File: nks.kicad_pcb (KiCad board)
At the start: 2 copper layers, 80 x 90 mm, 18 parts, among them J1 microSD, J2 DevKit-J1, J3 DevKit-J3, SW1 SW_Push, U2 RTC_DS3231+AT24C32, U3 SHT30

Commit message: feat(sw1): interruptor SPDT (SS12D00) rutado y verificado DRC 0; elimina R2 pull-up; anade libreria de footprints propia nks.pretty
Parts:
- removed R2: 10k, Resistor_SMD:R_0805_2012Metric
- SW1: value SW_Push -> SW_SPDT; footprint Button_Switch_THT:SW_PUSH_6mm -> nks:SS12D00
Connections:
- SW1 pad 1: /BTN -> /+3V3
- SW1 pad 2: /GND -> /BTN
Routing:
- net /+3V3: track 252.6 -> 245.5 mm
- net /BTN: track 234.4 -> 235.3 mm

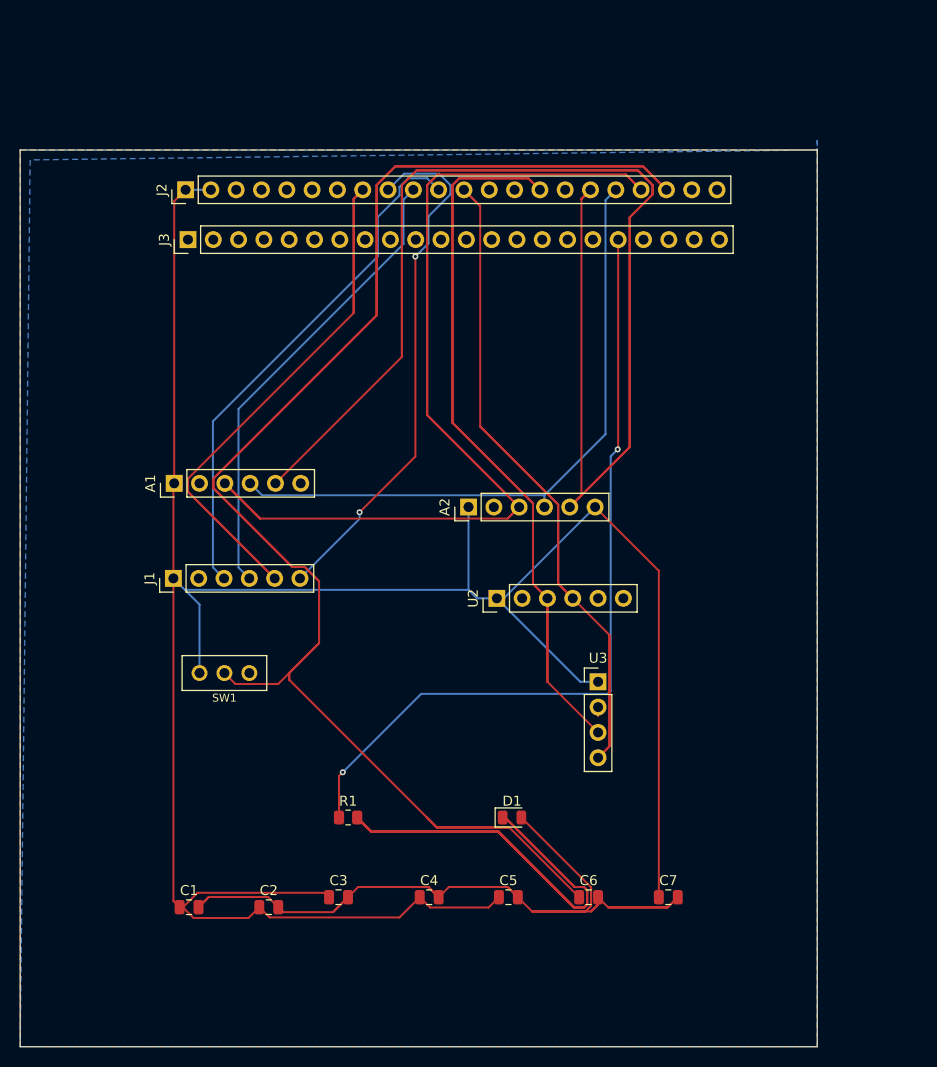
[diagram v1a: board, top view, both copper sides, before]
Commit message: layout: reconstruccion PCB desde esquematico nuevo - 20 componentes colocados, DevKit orientado USB trasero, panel LED+switch frontal
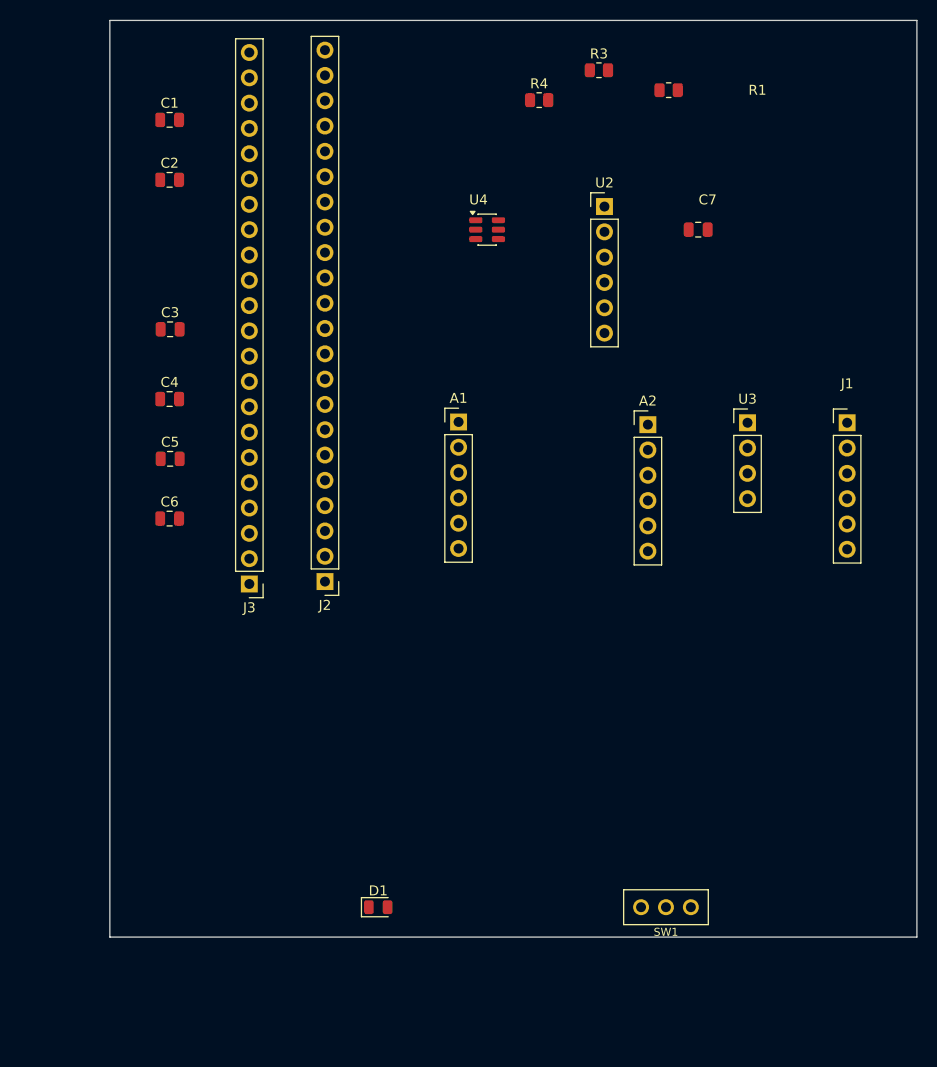
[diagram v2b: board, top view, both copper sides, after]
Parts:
- added R3: 100k, Resistor_SMD:R_0805_2012Metric, F.Cu at (149.1, 44.0)
- added R4: 100k, Resistor_SMD:R_0805_2012Metric, F.Cu at (143.1, 47.0)
- added U4: TPS22918, Package_TO_SOT_SMD:SOT-23-6, F.Cu at (137.9, 60.0)
- moved R1 79.8 mm to (156.1, 46.0)
- moved C1 79.0 mm to (106.0, 49.0)
- moved C2 73.7 mm to (106.0, 55.0)
- moved J1 69.4 mm to (174.0, 79.4), turned to 0 degrees
- moved C7 67.1 mm to (159.1, 60.0)
- moved C3 59.5 mm to (106.0, 70.0)
- moved C6 56.7 mm to (106.0, 89.0)
- moved C4 56.4 mm to (106.0, 77.0)
- moved C5 55.6 mm to (106.0, 83.0)
- moved SW1 50.2 mm to (155.8, 128.0)
- moved J2 41.7 mm to (121.6, 95.3), turned to 180 degrees
- moved U2 40.8 mm to (149.6, 57.7), turned to 0 degrees
- moved J3 35.1 mm to (114.0, 95.6), turned to 180 degrees
- moved U3 30.0 mm to (164.0, 79.4)
- moved A1 29.2 mm to (135.0, 79.3), turned to 0 degrees
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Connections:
- A1 pad 1: /+3V3 -> /+3V3_SW
- A2 pad 1: /+3V3 -> /+3V3_SW
- A2 pad 6: /+3V3 -> /+3V3_SW
- C1 pad 1: /+3V3 -> /+3V3_SW
- C2 pad 1: /+3V3 -> /+3V3_SW
- C3 pad 1: /+3V3 -> /+3V3_SW
- C4 pad 1: /+3V3 -> /+3V3_SW
- C5 pad 1: /+3V3 -> /+3V3_SW
- C7 pad 1: /+3V3 -> /+3V3_IN
- J1 pad 1: /+3V3 -> /+3V3_SW
- J2 pad 1: /+3V3 -> /+3V3_IN
- J2 pad 2: /+3V3 -> /+3V3_IN
- J2 pad 21: (no net) -> /VBUS
- J2 pad 4: (no net) -> /ENABLE
- J2 pad 5: (no net) -> /VBUS_ADC
- SW1 pad 1: /+3V3 -> /+3V3_SW
- U2 pad 1: /+3V3 -> /+3V3_IN
- U3 pad 1: /+3V3 -> /+3V3_SW
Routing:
- net /+3V3: track 245.5 -> 0.00 mm
- net /BTN: track 235.3 -> 0.00 mm
- net /LED_A: track 235.2 -> 0.00 mm
- net /I2S_WS: track 212.4 -> 0.00 mm
- net /I2S_SD: track 136.7 -> 0.00 mm
- net /I2C_SCL: track 125.8 -> 0.00 mm
- net /GND: track 116.0 -> 0.00 mm
- net /I2C_SDA: track 99.7 -> 0.00 mm
- net /LED_STAT: track 80.6 -> 0.00 mm, vias 2 -> 0
- net /SD_MOSI: track 74.9 -> 0.00 mm
- net /I2S_SCK: track 65.6 -> 0.00 mm
- net /SD_MISO: track 53.1 -> 0.00 mm, vias 2 -> 0
- net /SD_CS: track 52.3 -> 0.00 mm
- net /SD_SCLK: track 46.7 -> 0.00 mm
- removed copper zone on B.Cu, net /GND
- removed copper zone on F.Cu, net /GND
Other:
- board size 80 x 90 mm -> 81 x 92 mm

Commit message: layout: planos GND ambas caras rellenados (58->38 sin conectar); recupera ficheros tras restauracion KiCad
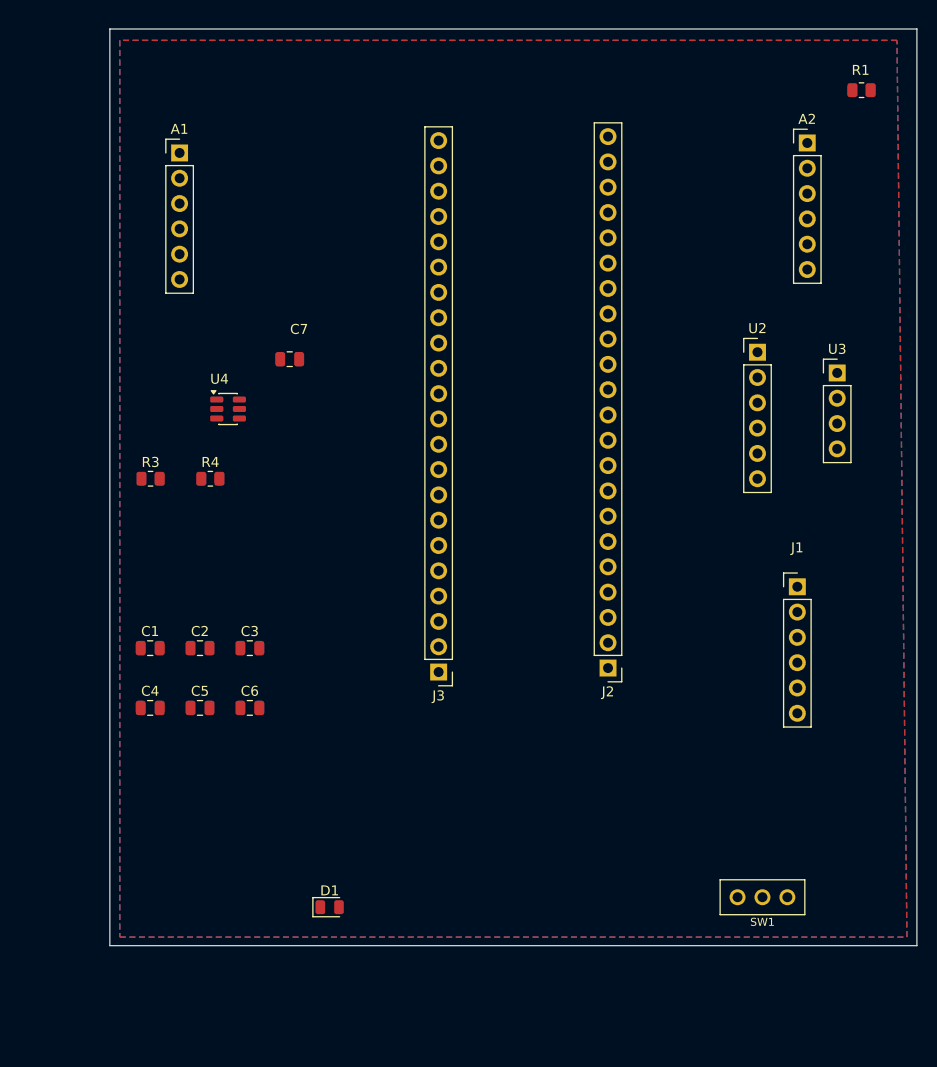
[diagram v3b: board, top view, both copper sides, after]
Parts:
- moved R3 60.9 mm to (104.1, 85.0)
- moved C1 53.1 mm to (104.0, 102.0)
- moved R4 50.3 mm to (110.1, 85.0)
- moved C2 47.1 mm to (109.0, 102.0)
- moved C7 43.0 mm to (118.0, 73.0)
- moved A1 38.9 mm to (107.0, 52.3)
- moved C3 33.0 mm to (114.0, 102.0)
- moved A2 32.5 mm to (170.0, 51.3)
- moved U4 31.6 mm to (111.9, 78.0)
- moved C4 31.1 mm to (104.0, 108.0)
- moved J2 29.7 mm to (150.0, 104.0)
- moved C5 25.2 mm to (109.0, 108.0)
- moved U2 21.2 mm to (165.0, 72.3)
- moved J3 21.0 mm to (133.0, 104.4)
- moved C6 20.6 mm to (114.0, 108.0)
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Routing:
- added copper zone on B.Cu, net /GND
- added copper zone on F.Cu, net /GND
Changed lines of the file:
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@@
 	(footprint "nks:SS12D00"
 		(layer "F.Cu")
-		(at 155.815 128)
+		(at 165.5 127)
 		(property "Reference" "SW1"
 			(at 0 2.5 0)
@@
 	(footprint "Capacitor_SMD:C_0805_2012Metric"
 		(layer "F.Cu")
-		(at 106 55)
+		(at 109.05 102)
 		(descr "Capacitor SMD 0805 (2012 Metric), square (rectangular) end terminal, IPC-7351 nominal, (Body size source: IPC-SM-782 page 76, https://www.pcb-3d.com/wordpress/wp-content/uploads/ipc-sm-782a_amendment_1_and_2.pdf, https://docs.google.com/spreadsheets/d/1BsfQQcO9C6DZCsRaXUlFlo91Tg2WpOkGARC1WS5S8t0/edit?usp=sharing)")
 		(tags "capacitor")
@@
 	(footprint "Connector_PinHeader_2.54mm:PinHeader_1x22_P2.54mm_Vertical"
 		(layer "F.Cu")
-		(at 114 95.56 180)
+		(at 133 104.4 180)
 		(descr "Through hole straight pin header, 1x22, 2.54mm pitch, single row")
 		(tags "Through hole pin header THT 1x22 2.54mm single row")
@@
 		)
 		(property "Value" "DevKit-J3"
-			(at 0 55.72 0)
+			(at 0 56.4 0)
 			(layer "F.Fab")
 			(effects
@@
 	(footprint "Connector_PinHeader_2.54mm:PinHeader_1x06_P2.54mm_Vertical"
 		(layer "F.Cu")
-		(at 135 79.3)
+		(at 107 52.3)
 		(descr "Through hole straight pin header, 1x06, 2.54mm pitch, single row")
 		(tags "Through hole pin header THT 1x06 2.54mm single row")
@@
 	(footprint "Connector_PinHeader_2.54mm:PinHeader_1x06_P2.54mm_Vertical"
 		(layer "F.Cu")
-		(at 174 79.38)
+		(at 169 95.84)
 		(descr "Through hole straight pin header, 1x06, 2.54mm pitch, single row")
 		(tags "Through hole pin header THT 1x06 2.54mm single row")
@@
 	(footprint "Connector_PinHeader_2.54mm:PinHeader_1x22_P2.54mm_Vertical"
 		(layer "F.Cu")
-		(at 121.59 95.32 180)
+		(at 150 104 180)
 		(descr "Through hole straight pin header, 1x22, 2.54mm pitch, single row")
 		(tags "Through hole pin header THT 1x22 2.54mm single row")
@@
 		)
 		(property "Value" "DevKit-J1"
-			(at 0 55.72 0)
+			(at 0 56 0)
 			(layer "F.Fab")
 			(effects
@@
 	(footprint "Connector_PinHeader_2.54mm:PinHeader_1x04_P2.54mm_Vertical"
 		(layer "F.Cu")
-		(at 164 79.38)
+		(at 173 74.38)
 		(descr "Through hole straight pin header, 1x04, 2.54mm pitch, single row")
 		(tags "Through hole pin header THT 1x04 2.54mm single row")
@@
 	(footprint "Resistor_SMD:R_0805_2012Metric"
 		(layer "F.Cu")
-		(at 143.0875 47)
+		(at 110.0875 85)
 		(descr "Resistor SMD 0805 (2012 Metric), square (rectangular) end terminal, IPC-7351 nominal, (Body size source: IPC-SM-782 page 72, https://www.pcb-3d.com/wordpress/wp-content/uploads/ipc-sm-782a_amendment_1_and_2.pdf)")
 		(tags "resistor")
@@
 	(footprint "Capacitor_SMD:C_0805_2012Metric"
 		(layer "F.Cu")
-		(at 106.05 70)
+		(at 114.05 102)
 		(descr "Capacitor SMD 0805 (2012 Metric), square (rectangular) end terminal, IPC-7351 nominal, (Body size source: IPC-SM-782 page 76, https://www.pcb-3d.com/wordpress/wp-content/uploads/ipc-sm-782a_amendment_1_and_2.pdf, https://docs.google.com/spreadsheets/d/1BsfQQcO9C6DZCsRaXUlFlo91Tg2WpOkGARC1WS5S8t0/edit?usp=sharing)")
 		(tags "capacitor")
@@
 	(footprint "Connector_PinHeader_2.54mm:PinHeader_1x06_P2.54mm_Vertical"
 		(layer "F.Cu")
-		(at 149.643748 57.68)
+		(at 165 72.3)
 		(descr "Through hole straight pin header, 1x06, 2.54mm pitch, single row")
 		(tags "Through hole pin header THT 1x06 2.54mm single row")
@@
 	(footprint "Package_TO_SOT_SMD:SOT-23-6"
 		(layer "F.Cu")
-		(at 137.8625 60)
+		(at 111.8625 78)
 		(descr "SOT, 6 Pin (JEDEC MO-178 Var AB https://www.jedec.org/document_search?search_api_views_fulltext=MO-178)")
 		(tags "SOT TO_SOT_SMD")
@@
 	(footprint "Resistor_SMD:R_0805_2012Metric"
 		(layer "F.Cu")
-		(at 149.0875 44)
+		(at 104.0875 85)
 		(descr "Resistor SMD 0805 (2012 Metric), square (rectangular) end terminal, IPC-7351 nominal, (Body size source: IPC-SM-782 page 72, https://www.pcb-3d.com/wordpress/wp-content/uploads/ipc-sm-782a_amendment_1_and_2.pdf)")
 		(tags "resistor")
@@
 	(footprint "Capacitor_SMD:C_0805_2012Metric"
 		(layer "F.Cu")
-		(at 106 89)
+		(at 114.05 108)
 		(descr "Capacitor SMD 0805 (2012 Metric), square (rectangular) end terminal, IPC-7351 nominal, (Body size source: IPC-SM-782 page 76, https://www.pcb-3d.com/wordpress/wp-content/uploads/ipc-sm-782a_amendment_1_and_2.pdf, https://docs.google.com/spreadsheets/d/1BsfQQcO9C6DZCsRaXUlFlo91Tg2WpOkGARC1WS5S8t0/edit?usp=sharing)")
 		(tags "capacitor")
@@
 	(footprint "LED_SMD:LED_0805_2012Metric"
 		(layer "F.Cu")
-		(at 126.9375 128)
+		(at 122.0625 128)
 		(descr "LED SMD 0805 (2012 Metric), square (rectangular) end terminal, IPC-7351 nominal, (Body size source: https://docs.google.com/spreadsheets/d/1BsfQQcO9C6DZCsRaXUlFlo91Tg2WpOkGARC1WS5S8t0/edit?usp=sharing)")
 		(tags "LED")
@@
 	(footprint "Resistor_SMD:R_0805_2012Metric"
 		(layer "F.Cu")
-		(at 156.0875 46)
+		(at 175.443752 46)
 		(descr "Resistor SMD 0805 (2012 Metric), square (rectangular) end terminal, IPC-7351 nominal, (Body size source: IPC-SM-782 page 72, https://www.pcb-3d.com/wordpress/wp-content/uploads/ipc-sm-782a_amendment_1_and_2.pdf)")
 		(tags "resistor")
 		(property "Reference" "R1"
-			(at 8.9125 0 0)
+			(at -0.0875 -2 0)
 			(layer "F.SilkS")
 			(effects
@@
 	(footprint "Connector_PinHeader_2.54mm:PinHeader_1x06_P2.54mm_Vertical"
 		(layer "F.Cu")
-		(at 154 79.57)
+		(at 170 51.3)
 		(descr "Through hole straight pin header, 1x06, 2.54mm pitch, single row")
 		(tags "Through hole pin header THT 1x06 2.54mm single row")
@@
 	(footprint "Capacitor_SMD:C_0805_2012Metric"
 		(layer "F.Cu")
-		(at 106 77)
+		(at 104.05 108)
 		(descr "Capacitor SMD 0805 (2012 Metric), square (rectangular) end terminal, IPC-7351 nominal, (Body size source: IPC-SM-782 page 76, https://www.pcb-3d.com/wordpress/wp-content/uploads/ipc-sm-782a_amendment_1_and_2.pdf, https://docs.google.com/spreadsheets/d/1BsfQQcO9C6DZCsRaXUlFlo91Tg2WpOkGARC1WS5S8t0/edit?usp=sharing)")
 		(tags "capacitor")
@@
 	(footprint "Capacitor_SMD:C_0805_2012Metric"
 		(layer "F.Cu")
-		(at 106.05 83)
+		(at 109.05 108)
 		(descr "Capacitor SMD 0805 (2012 Metric), square (rectangular) end terminal, IPC-7351 nominal, (Body size source: IPC-SM-782 page 76, https://www.pcb-3d.com/wordpress/wp-content/uploads/ipc-sm-782a_amendment_1_and_2.pdf, https://docs.google.com/spreadsheets/d/1BsfQQcO9C6DZCsRaXUlFlo91Tg2WpOkGARC1WS5S8t0/edit?usp=sharing)")
 		(tags "capacitor")
@@
 	(footprint "Capacitor_SMD:C_0805_2012Metric"
 		(layer "F.Cu")
-		(at 106 48.98)
+		(at 104.05 102)
 		(descr "Capacitor SMD 0805 (2012 Metric), square (rectangular) end terminal, IPC-7351 nominal, (Body size source: IPC-SM-782 page 76, https://www.pcb-3d.com/wordpress/wp-content/uploads/ipc-sm-782a_amendment_1_and_2.pdf, https://docs.google.com/spreadsheets/d/1BsfQQcO9C6DZCsRaXUlFlo91Tg2WpOkGARC1WS5S8t0/edit?usp=sharing)")
 		(tags "capacitor")
@@
 	(footprint "Capacitor_SMD:C_0805_2012Metric"
 		(layer "F.Cu")
-		(at 159.05 60)
+		(at 118.05 73)
 		(descr "Capacitor SMD 0805 (2012 Metric), square (rectangular) end terminal, IPC-7351 nominal, (Body size source: IPC-SM-782 page 76, https://www.pcb-3d.com/wordpress/wp-content/uploads/ipc-sm-782a_amendment_1_and_2.pdf, https://docs.google.com/spreadsheets/d/1BsfQQcO9C6DZCsRaXUlFlo91Tg2WpOkGARC1WS5S8t0/edit?usp=sharing)")
 		(tags "capacitor")
@@
 	)
 	(gr_rect
-		(start 100 39)
-		(end 181 131)
+		(start 100 39.86)
+		(end 181 131.86)
 		(stroke
 			(width 0.1)
@@
 		(layer "Edge.Cuts")
 	)
+	(zone
+		(net "/GND")
+		(layer "F.Cu")
+		(hatch edge 0.5)
+		(connect_pads
+			(clearance 0.5)
+		)
+		(min_thickness 0.25)
+		(fill yes
+			(thermal_gap 0.5)
+			(thermal_bridge_width 0.5)
+			(island_removal_mode 0)
+		)
+		(polygon
+			(pts
+				(xy 101 41) (xy 101 131) (xy 180 131) (xy 179 41)
+			)
+		)
+	)
+	(zone
+		(net "/GND")
+		(layer "B.Cu")
+		(hatch edge 0.5)
+		(priority 1)
+		(connect_pads
+			(clearance 0.5)
+		)
+		(min_thickness 0.25)
+		(fill yes
+			(thermal_gap 0.5)
+			(thermal_bridge_width 0.5)
+			(island_removal_mode 0)
+		)
+		(polygon
+			(pts
+				(xy 101 41) (xy 101 131) (xy 180 131) (xy 179 41)
+			)
+		)
+	)
 	(embedded_fonts no)

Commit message: Rutado completo de señales y alimentación (0 violaciones, pendiente costura GND)
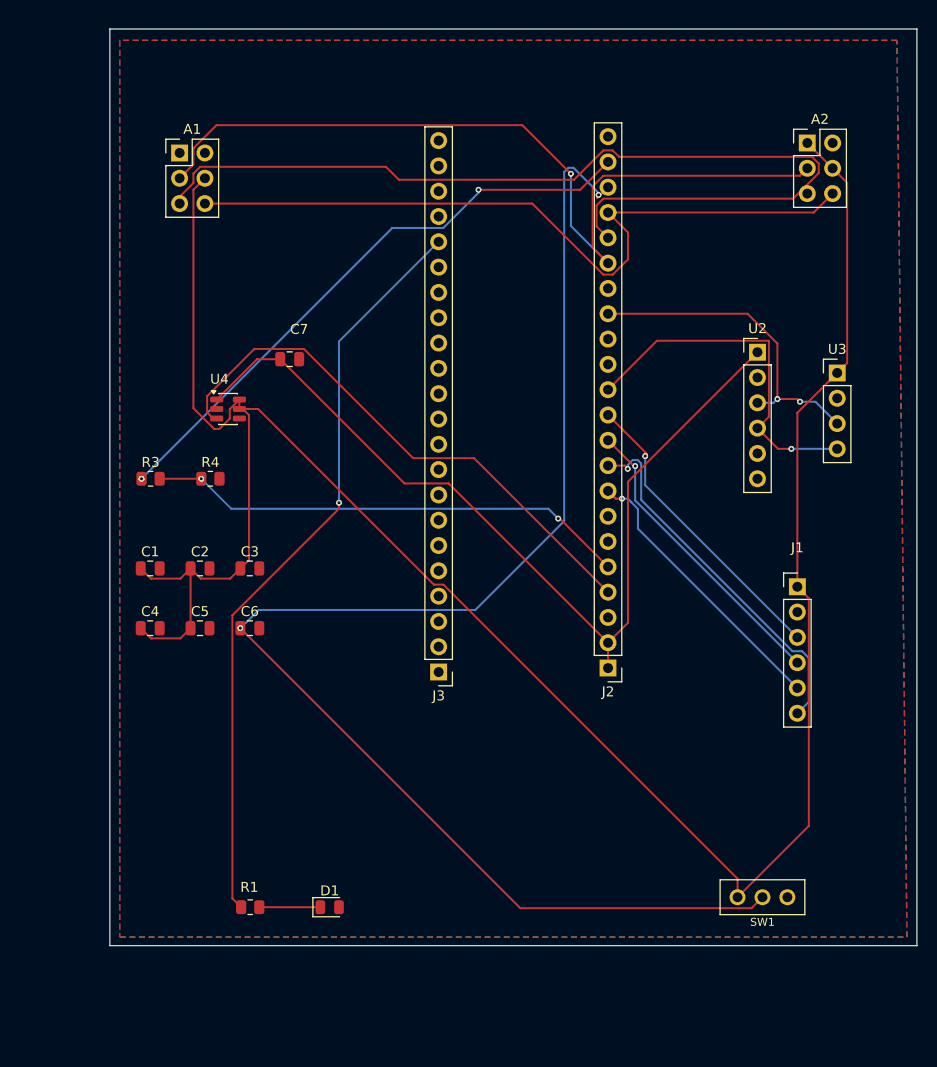
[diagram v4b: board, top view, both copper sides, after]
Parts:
- A1, A2: footprint Connector_PinHeader_2.54mm:PinHeader_1x06_P2.54mm_Vertical -> Connector_PinHeader_2.54mm:PinHeader_2x03_P2.54mm_Vertical
- moved R1 102.4 mm to (114.1, 128.0)
- moved C1 8.00 mm to (104.0, 94.0)
- moved C2 8.00 mm to (109.0, 94.0)
- moved C3 8.00 mm to (114.0, 94.0)
- moved C4 8.00 mm to (104.0, 100.0)
- moved C5 8.00 mm to (109.0, 100.0)
- moved C6 8.00 mm to (114.0, 100.0)
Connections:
- A1 pad 1: /+3V3_SW -> /GND
- A1 pad 3: /I2S_SD -> /I2S_WS
- A1 pad 4: /I2S_SCK -> /+3V3_SW
- A1 pad 5: /I2S_WS -> /I2S_SCK
- A1 pad 6: /GND -> /I2S_SD
- A2 pad 3: /I2S_SD -> /I2S_WS
- A2 pad 4: /I2S_SCK -> /+3V3_SW
- A2 pad 5: /I2S_WS -> /I2S_SCK
- A2 pad 6: /+3V3_SW -> /I2S_SD
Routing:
- net /+3V3_SW: track 0.00 -> 226.5 mm
- net /BTN: track 0.00 -> 143.2 mm, vias 0 -> 2
- net /I2S_SCK: track 0.00 -> 97.3 mm
- net /+3V3_IN: track 0.00 -> 90.7 mm
- net /I2S_WS: track 0.00 -> 86.0 mm, vias 0 -> 1
- net /LED_STAT: track 0.00 -> 75.7 mm, vias 0 -> 2
- net /I2S_SD: track 0.00 -> 74.9 mm
- net /VBUS: track 0.00 -> 60.2 mm, vias 0 -> 2
- net /ENABLE: track 0.00 -> 55.2 mm
- net /VBUS_ADC: track 0.00 -> 48.7 mm, vias 0 -> 2
- net /SD_MISO: track 0.00 -> 37.3 mm, vias 0 -> 1
- net /I2C_SDA: track 0.00 -> 36.3 mm, vias 0 -> 1
- net /I2C_SCL: track 0.00 -> 33.0 mm, vias 0 -> 2
- net /SD_SCLK: track 0.00 -> 30.7 mm, vias 0 -> 1
- net /SD_CS: track 0.00 -> 30.6 mm, vias 0 -> 1
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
